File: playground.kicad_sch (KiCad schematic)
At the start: 50 parts, among them IC11 LM3940IMP-3.3_NOPB, IC9 L293DD, J1 67643-2910, J2 Pump, J3 Fan, J4 Valve, J5 Conn_02x05_Counter_Clockwise, J6 MOLEX POWER CONNECTOR, SW1 SW_DIP_x01, U2 ATSAMD21G18A-A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

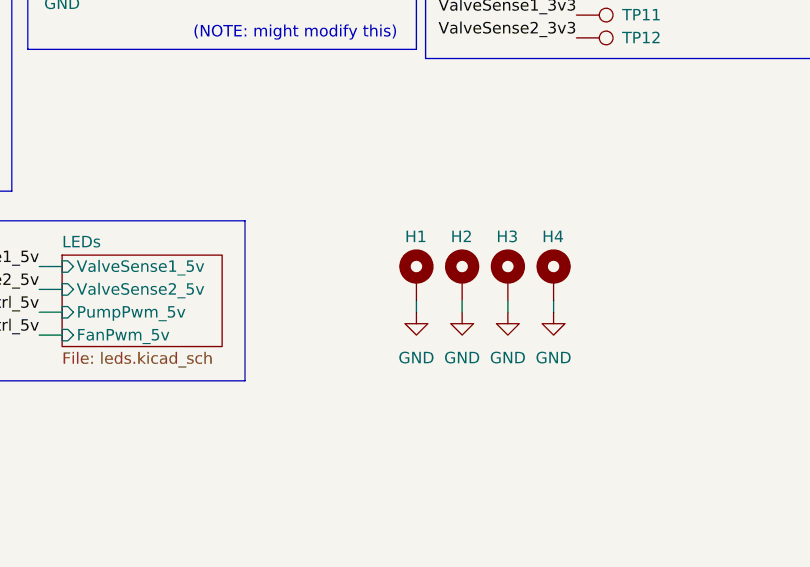
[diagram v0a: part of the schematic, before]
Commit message: Layout and Route of 4 layer version complete.
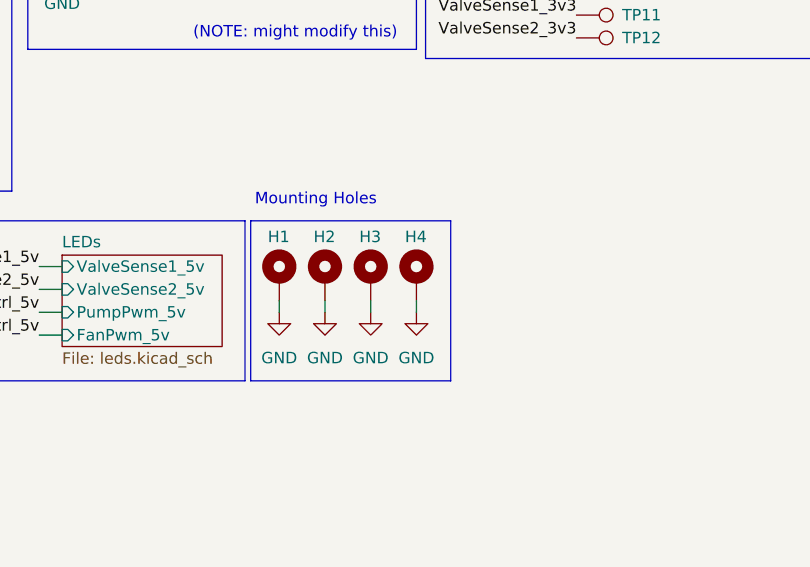
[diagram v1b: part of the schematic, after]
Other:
- note added: "Mounting Holes"
- moved on the sheet: H1, H2, H3, H4
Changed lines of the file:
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@@
 	(wire
 		(pts
-			(xy 255.27 118.11) (xy 255.27 119.38)
+			(xy 240.03 118.11) (xy 240.03 119.38)
 		)
 		(stroke
@@
 	(wire
 		(pts
-			(xy 245.11 118.11) (xy 245.11 119.38)
+			(xy 229.87 118.11) (xy 229.87 119.38)
 		)
 		(stroke
@@
 	(wire
 		(pts
-			(xy 250.19 118.11) (xy 250.19 119.38)
+			(xy 234.95 118.11) (xy 234.95 119.38)
 		)
 		(stroke
@@
 	(wire
 		(pts
-			(xy 240.03 118.11) (xy 240.03 119.38)
+			(xy 224.79 118.11) (xy 224.79 119.38)
 		)
 		(stroke
@@
 	)
 	(rectangle
+		(start 221.615 109.22)
+		(end 243.84 127)
+		(stroke
+			(width 0)
+			(type default)
+		)
+		(fill
+			(type none)
+		)
+	)
+	(rectangle
 		(start 182.245 109.22)
 		(end 220.98 127)
@@
 		)
 	)
+	(text "Mounting Holes"
+		(exclude_from_sim no)
+		(at 228.854 106.934 0)
+		(effects
+			(font
+				(size 1.27 1.27)
+			)
+		)
+	)
 	(text "ANA"
 		(exclude_from_sim no)
@@
 	(symbol
 		(lib_id "Mechanical:MountingHole_Pad")
-		(at 250.19 115.57 0)
+		(at 234.95 115.57 0)
 		(unit 1)
 		(exclude_from_sim no)
@@
 		(dnp no)
 		(property "Reference" "H3"
-			(at 248.92 110.998 0)
+			(at 233.68 110.998 0)
 			(effects
 				(font
@@
 		)
 		(property "Value" "MountingHole_Pad"
-			(at 252.73 115.5699 0)
+			(at 237.49 115.5699 0)
 			(effects
 				(font
@@
 		)
 		(property "Footprint" "MountingHole:MountingHole_2.2mm_M2_Pad"
-			(at 250.19 115.57 0)
+			(at 234.95 115.57 0)
 			(effects
 				(font
@@
 		)
 		(property "Datasheet" "~"
-			(at 250.19 115.57 0)
+			(at 234.95 115.57 0)
 			(effects
 				(font
@@
 		)
 		(property "Description" "Mounting Hole with connection"
-			(at 250.19 115.57 0)
+			(at 234.95 115.57 0)
 			(effects
 				(font
@@
 	(symbol
 		(lib_id "power:GND")
-		(at 240.03 119.38 0)
+		(at 224.79 119.38 0)
 		(unit 1)
 		(exclude_from_sim no)
@@
 		(fields_autoplaced yes)
 		(property "Reference" "#PWR056"
-			(at 240.03 125.73 0)
+			(at 224.79 125.73 0)
 			(effects
 				(font
@@
 		)
 		(property "Value" "GND"
-			(at 240.03 124.46 0)
+			(at 224.79 124.46 0)
 			(effects
 				(font
@@
 		)
 		(property "Footprint" ""
-			(at 240.03 119.38 0)
+			(at 224.79 119.38 0)
 			(effects
 				(font
@@
 		)
 		(property "Datasheet" ""
-			(at 240.03 119.38 0)
+			(at 224.79 119.38 0)
 			(effects
 				(font
@@
 		)
 		(property "Description" "Power symbol creates a global label with name \"GND\" , ground"
-			(at 240.03 119.38 0)
+			(at 224.79 119.38 0)
 			(effects
 				(font
@@
 	(symbol
 		(lib_id "Mechanical:MountingHole_Pad")
-		(at 240.03 115.57 0)
+		(at 224.79 115.57 0)
 		(unit 1)
 		(exclude_from_sim no)
@@
 		(dnp no)
 		(property "Reference" "H1"
-			(at 238.76 110.998 0)
+			(at 223.52 110.998 0)
 			(effects
 				(font
@@
 		)
 		(property "Value" "MountingHole_Pad"
-			(at 242.57 115.5699 0)
+			(at 227.33 115.5699 0)
 			(effects
 				(font
@@
 		)
 		(property "Footprint" "MountingHole:MountingHole_2.2mm_M2_Pad"
-			(at 240.03 115.57 0)
+			(at 224.79 115.57 0)
 			(effects
 				(font
@@
 		)
 		(property "Datasheet" "~"
-			(at 240.03 115.57 0)
+			(at 224.79 115.57 0)
 			(effects
 				(font
@@
 		)
 		(property "Description" "Mounting Hole with connection"
-			(at 240.03 115.57 0)
+			(at 224.79 115.57 0)
 			(effects
 				(font
@@
 	(symbol
 		(lib_id "Mechanical:MountingHole_Pad")
-		(at 245.11 115.57 0)
+		(at 229.87 115.57 0)
 		(unit 1)
 		(exclude_from_sim no)
@@
 		(dnp no)
 		(property "Reference" "H2"
-			(at 243.84 110.998 0)
+			(at 228.6 110.998 0)
 			(effects
 				(font
@@
 		)
 		(property "Value" "MountingHole_Pad"
-			(at 247.65 115.5699 0)
+			(at 232.41 115.5699 0)
 			(effects
 				(font
@@
 		)
 		(property "Footprint" "MountingHole:MountingHole_2.2mm_M2_Pad"
-			(at 245.11 115.57 0)
+			(at 229.87 115.57 0)
 			(effects
 				(font
@@
 		)
 		(property "Datasheet" "~"
-			(at 245.11 115.57 0)
+			(at 229.87 115.57 0)
 			(effects
 				(font
@@
 		)
 		(property "Description" "Mounting Hole with connection"
-			(at 245.11 115.57 0)
+			(at 229.87 115.57 0)
 			(effects
 				(font
@@
 	(symbol
 		(lib_id "power:GND")
-		(at 245.11 119.38 0)
+		(at 229.87 119.38 0)
 		(unit 1)
 		(exclude_from_sim no)
@@
 		(fields_autoplaced yes)
 		(property "Reference" "#PWR057"
-			(at 245.11 125.73 0)
+			(at 229.87 125.73 0)
 			(effects
 				(font
@@
 		)
 		(property "Value" "GND"
-			(at 245.11 124.46 0)
+			(at 229.87 124.46 0)
 			(effects
 				(font
@@
 		)
 		(property "Footprint" ""
-			(at 245.11 119.38 0)
+			(at 229.87 119.38 0)
 			(effects
 				(font
@@
 		)
 		(property "Datasheet" ""
-			(at 245.11 119.38 0)
+			(at 229.87 119.38 0)
 			(effects
 				(font
@@
 		)
 		(property "Description" "Power symbol creates a global label with name \"GND\" , ground"
-			(at 245.11 119.38 0)
+			(at 229.87 119.38 0)
 			(effects
 				(font
@@
 	(symbol
 		(lib_id "power:GND")
-		(at 250.19 119.38 0)
+		(at 234.95 119.38 0)
 		(unit 1)
 		(exclude_from_sim no)
@@
 		(fields_autoplaced yes)
 		(property "Reference" "#PWR058"
-			(at 250.19 125.73 0)
+			(at 234.95 125.73 0)
 			(effects
 				(font
@@
 		)
 		(property "Value" "GND"
-			(at 250.19 124.46 0)
+			(at 234.95 124.46 0)
 			(effects
 				(font
@@
 		)
 		(property "Footprint" ""
-			(at 250.19 119.38 0)
+			(at 234.95 119.38 0)
 			(effects
 				(font
@@
 		)
 		(property "Datasheet" ""
-			(at 250.19 119.38 0)
+			(at 234.95 119.38 0)
 			(effects
 				(font
@@
 		)
 		(property "Description" "Power symbol creates a global label with name \"GND\" , ground"
-			(at 250.19 119.38 0)
+			(at 234.95 119.38 0)
 			(effects
 				(font
@@
 	(symbol
 		(lib_id "Mechanical:MountingHole_Pad")
-		(at 255.27 115.57 0)
+		(at 240.03 115.57 0)
 		(unit 1)
 		(exclude_from_sim no)
@@
 		(dnp no)
 		(property "Reference" "H4"
-			(at 254 110.998 0)
+			(at 238.76 110.998 0)
 			(effects
 				(font
@@
 		)
 		(property "Value" "MountingHole_Pad"
-			(at 257.81 115.5699 0)
+			(at 242.57 115.5699 0)
 			(effects
 				(font
@@
 		)
 		(property "Footprint" "MountingHole:MountingHole_2.2mm_M2_Pad"
-			(at 255.27 115.57 0)
+			(at 240.03 115.57 0)
 			(effects
 				(font
@@
 		)
 		(property "Datasheet" "~"
-			(at 255.27 115.57 0)
+			(at 240.03 115.57 0)
 			(effects
 				(font
@@
 		)
 		(property "Description" "Mounting Hole with connection"
-			(at 255.27 115.57 0)
+			(at 240.03 115.57 0)
 			(effects
 				(font
@@
 	(symbol
 		(lib_id "power:GND")
-		(at 255.27 119.38 0)
+		(at 240.03 119.38 0)
 		(unit 1)
 		(exclude_from_sim no)
@@
 		(fields_autoplaced yes)
 		(property "Reference" "#PWR059"
-			(at 255.27 125.73 0)
+			(at 240.03 125.73 0)
 			(effects
 				(font
@@
 		)
 		(property "Value" "GND"
-			(at 255.27 124.46 0)
+			(at 240.03 124.46 0)
 			(effects
 				(font
@@
 		)
 		(property "Footprint" ""
-			(at 255.27 119.38 0)
+			(at 240.03 119.38 0)
 			(effects
 				(font
@@
 		)
 		(property "Datasheet" ""
-			(at 255.27 119.38 0)
+			(at 240.03 119.38 0)
 			(effects
 				(font
@@
 		)
 		(property "Description" "Power symbol creates a global label with name \"GND\" , ground"
-			(at 255.27 119.38 0)
+			(at 240.03 119.38 0)
 			(effects
 				(font

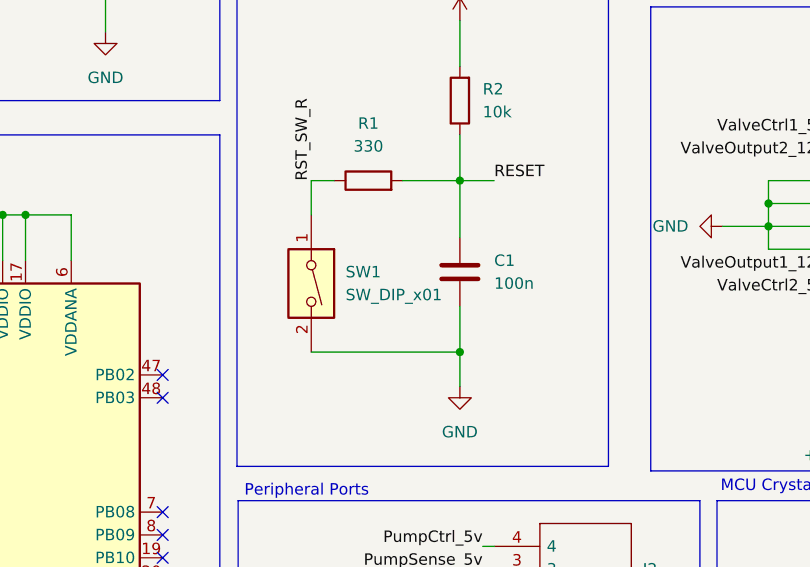
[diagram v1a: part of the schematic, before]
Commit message: Modified layout. Added more silkscreen.
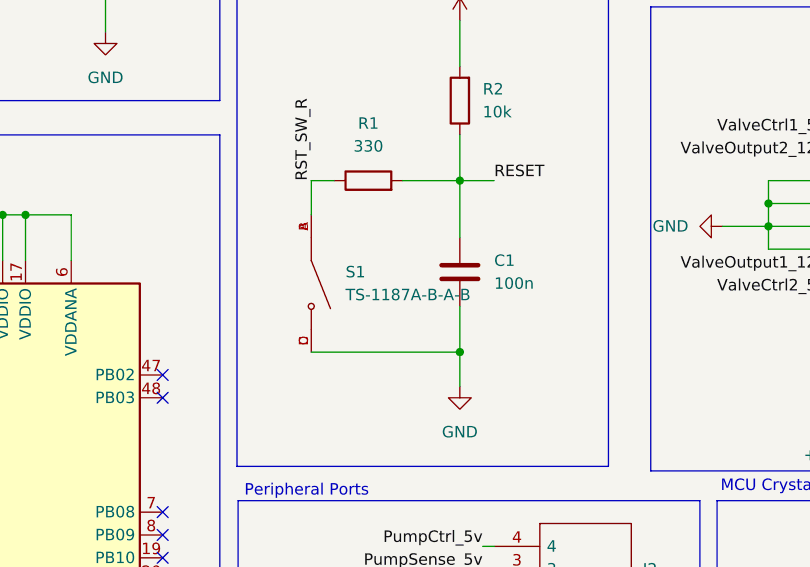
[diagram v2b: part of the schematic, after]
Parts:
- removed SW1: SW_DIP_x01, Button_Switch_SMD:SW_Push_1TS009xxxx-xxxx-xxxx_6x6x5mm, symbol Switch:SW_DIP_x01
- added S1: TS-1187A-B-A-B, custom_footprints:SW_TS-1187A-B-A-B, symbol custom_symbols:TS-1187A-B-A-B
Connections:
- net GND: now also S1.C, S1.D
- net RST_SW_R: now also S1.A, S1.B
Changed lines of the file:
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@@
-	)
-	(symbol
-		(lib_id "Switch:SW_DIP_x01")
-		(at 87.63 85.09 270)
-		(unit 1)
-		(exclude_from_sim no)
-		(in_bom yes)
-		(on_board yes)
-		(dnp no)
-		(fields_autoplaced yes)
-		(property "Reference" "SW1"
-			(at 91.44 83.8199 90)
-			(effects
-				(font
-					(size 1.27 1.27)
-				)
-				(justify left)
-			)
-		)
-		(property "Value" "SW_DIP_x01"
-			(at 91.44 86.3599 90)
-			(effects
-				(font
-					(size 1.27 1.27)
-				)
-				(justify left)
-			)
-		)
-		(property "Footprint" "Button_Switch_SMD:SW_Push_1TS009xxxx-xxxx-xxxx_6x6x5mm"
-			(at 87.63 85.09 0)
-			(effects
-				(font
-					(size 1.27 1.27)
-				)
-				(hide yes)
-			)
-		)
-		(property "Datasheet" "~"
-			(at 87.63 85.09 0)
-			(effects
-				(font
-					(size 1.27 1.27)
-				)
-				(hide yes)
-			)
-		)
-		(property "Description" "1x DIP Switch, Single Pole Single Throw (SPST) switch, small symbol"
-			(at 87.63 85.09 0)
-			(effects
-				(font
-					(size 1.27 1.27)
-				)
-				(hide yes)
-			)
-		)
-		(pin "2"
-		)
-		(pin "1"
-		)
-		(instances
-			(project "playground"
-				(path "/e7dc7c2b-347f-4a52-91f1-4651868a2780"
-					(reference "SW1")
-					(unit 1)
-				)
-			)
-		)
 	)
 	(symbol
@@
 					(unit 1)
 				)
+			)
+		)
+	)
+	(symbol
+		(lib_id "custom_symbols:TS-1187A-B-A-B")
+		(at 87.63 85.09 270)
+		(unit 1)
+		(exclude_from_sim no)
+		(in_bom yes)
+		(on_board yes)
+		(dnp no)
+		(fields_autoplaced yes)
+		(property "Reference" "S1"
+			(at 91.44 83.8199 90)
+			(effects
+				(font
+					(size 1.27 1.27)
+				)
+				(justify left)
+			)
+		)
+		(property "Value" "TS-1187A-B-A-B"
+			(at 91.44 86.3599 90)
+			(effects
+				(font
+					(size 1.27 1.27)
+				)
+				(justify left)
+			)
+		)
+		(property "Footprint" "custom_footprints:SW_TS-1187A-B-A-B"
+			(at 87.63 85.09 0)
+			(effects
+				(font
+					(size 1.27 1.27)
+				)
+				(justify bottom)
+				(hide yes)
+			)
+		)
+		(property "Datasheet" ""
+			(at 87.63 85.09 0)
+			(effects
+				(font
+					(size 1.27 1.27)
+				)
+				(hide yes)
+			)
+		)
+		(property "Description" ""
+			(at 87.63 85.09 0)
+			(effects
+				(font
+					(size 1.27 1.27)
+				)
+				(hide yes)
+			)
+		)
+		(property "MF" "XKB Industrial Precision"
+			(at 87.63 85.09 0)
+			(effects
+				(font
+					(size 1.27 1.27)
+				)
+				(justify bottom)
+				(hide yes)
+			)
+		)
+		(property "MAXIMUM_PACKAGE_HEIGHT" "1.5mm"
+			(at 87.63 85.09 0)
+			(effects
+				(font
+					(size 1.27 1.27)
+				)
+				(justify bottom)
+				(hide yes)
+			)
+		)
+		(property "Package" "Package"
+			(at 87.63 85.09 0)
+			(effects
+				(font
+					(size 1.27 1.27)
+				)
+				(justify bottom)
+				(hide yes)
+			)
+		)
+		(property "Price" "None"
+			(at 87.63 85.09 0)
+			(effects
+				(font
+					(size 1.27 1.27)
+				)
+				(justify bottom)
+				(hide yes)
+			)
+		)
+		(property "Check_prices" "https://www.snapeda.com/parts/TS-1187A-B-A-B/XKB+Industrial+Precision/view-part/?ref=eda"
+			(at 87.63 85.09 0)
+			(effects
+				(font
+					(size 1.27 1.27)
+				)
+				(justify bottom)
+				(hide yes)
+			)
+		)
+		(property "STANDARD" "Manufacturer Recommendations"
+			(at 87.63 85.09 0)
+			(effects
+				(font
+					(size 1.27 1.27)
+				)
+				(justify bottom)
+				(hide yes)
+			)
+		)
+		(property "PARTREV" "A0"
+			(at 87.63 85.09 0)
+			(effects
+				(font
+					(size 1.27 1.27)
+				)
+				(justify bottom)
+				(hide yes)
+			)
+		)
+		(property "SnapEDA_Link" "https://www.snapeda.com/parts/TS-1187A-B-A-B/XKB+Industrial+Precision/view-part/?ref=snap"
+			(at 87.63 85.09 0)
+			(effects
+				(font
+					(size 1.27 1.27)
+				)
+				(justify bottom)
+				(hide yes)
+			)
+		)
+		(property "MP" "TS-1187A-B-A-B"
+			(at 87.63 85.09 0)
+			(effects
+				(font
+					(size 1.27 1.27)
+				)
+				(justify bottom)
+				(hide yes)
+			)
+		)
+		(property "Description_1" "\nTS-1187A-B-A-B XKB Connectivity\n"
+			(at 87.63 85.09 0)
+			(effects
+				(font
+					(size 1.27 1.27)
+				)
+				(justify bottom)
+				(hide yes)
+			)
+		)
+		(property "Availability" "Not in stock"
+			(at 87.63 85.09 0)
+			(effects
+				(font
+					(size 1.27 1.27)
+				)
+				(justify bottom)
+				(hide yes)
+			)
+		)
+		(property "MANUFACTURER" "XKB Industrial Precision"
+			(at 87.63 85.09 0)
+			(effects
+				(font
+					(size 1.27 1.27)
+				)
+				(justify bottom)
+				(hide yes)
+			)
+		)
+		(pin "D"
+		)
+		(pin "B"
+		)
+		(pin "A"
+		)
+		(pin "C"
+		)
+		(instances
+			(project "playground"
+				(path "/e7dc7c2b-347f-4a52-91f1-4651868a2780"
+					(reference "S1")
+					(unit 1)
+				)
